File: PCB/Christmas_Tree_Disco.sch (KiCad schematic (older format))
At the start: 0 parts

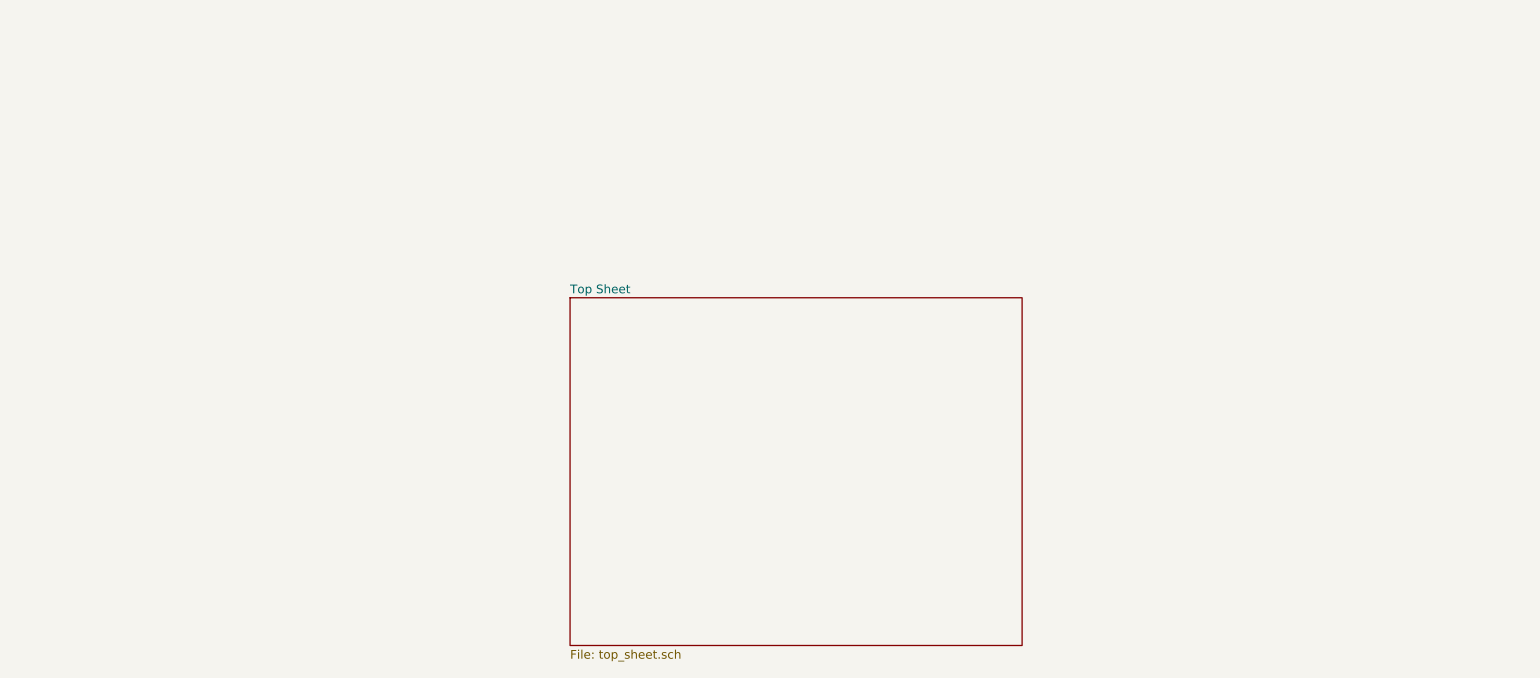
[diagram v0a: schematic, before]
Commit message: PCB Edge.Cuts Defined
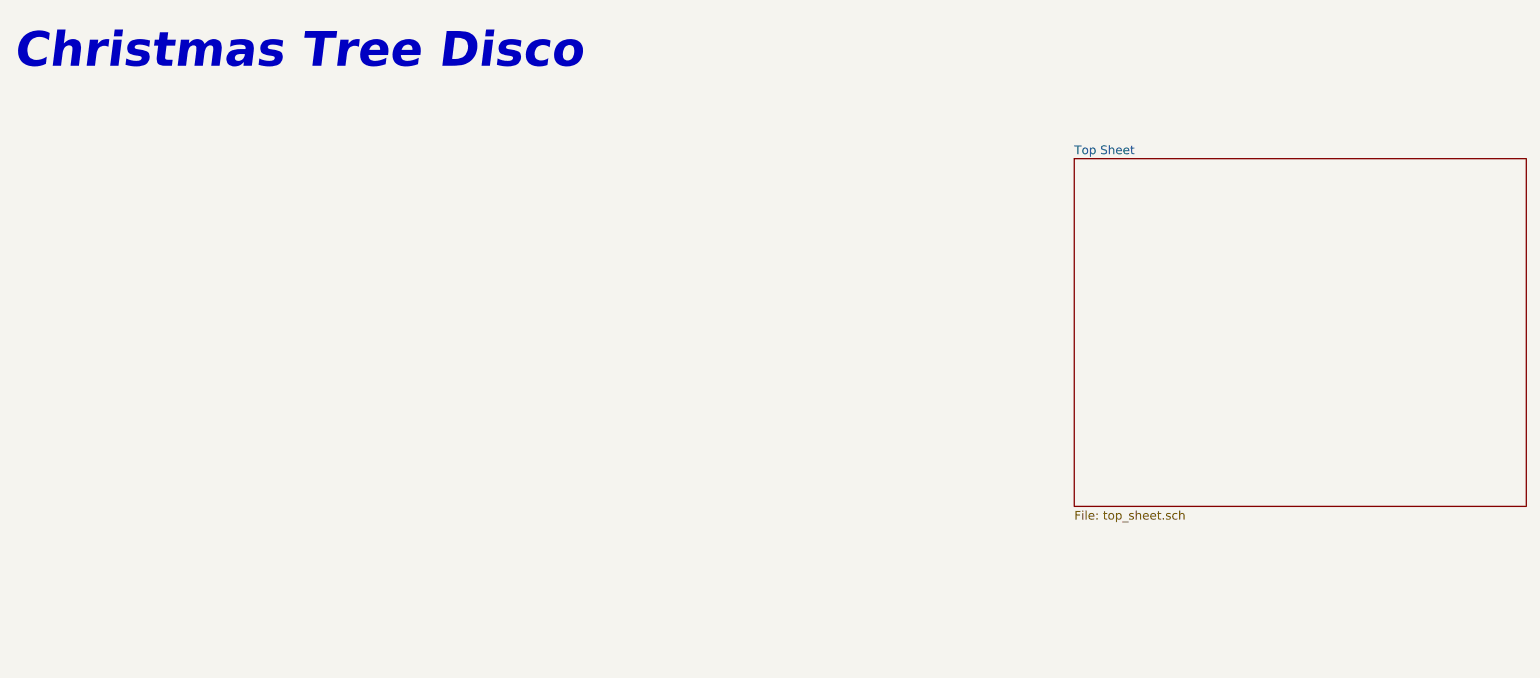
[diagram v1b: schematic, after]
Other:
- note added: "Christmas Tree Disco"
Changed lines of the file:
@@
 $Descr A 11000 8500
 encoding utf-8
-Sheet 1 5
+Sheet 1 20
 Title "Christmas Tree Disco"
 Date "2017-08-01"
 Rev "01"
-Comp "GitHub/Cryochasm"
+Comp "www.GitHub.com/Cryochasm"
 Comment1 ""
 Comment2 ""
@@
 $EndDescr
 $Sheet
-S 4000 2400 2600 2000
+S 6900 1600 2600 2000
 U 59809489
 F0 "Top Sheet" 50
 F1 "top_sheet.sch" 50
 $EndSheet
+Text Notes 800  1100 0    200  Italic 40
+Christmas Tree Disco
 $EndSCHEMATC

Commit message: Preliminary PCB layout
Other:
- note added: "Revisions:"
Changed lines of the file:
@@
 Text Notes 800  1100 0    200  Italic 40
 Christmas Tree Disco
+Text Notes 1000 1400 0    50   ~ 0
+Revisions:
 $EndSCHEMATC

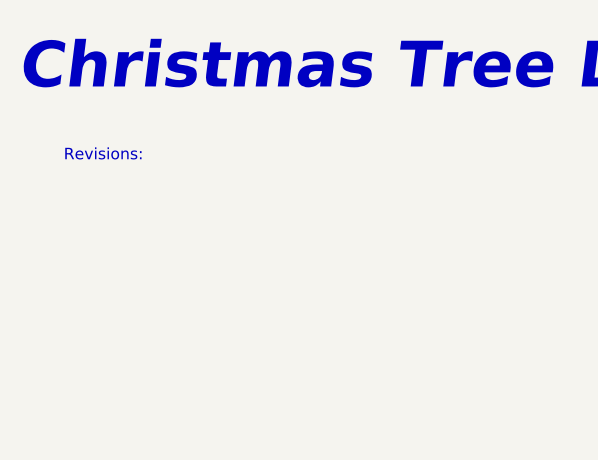
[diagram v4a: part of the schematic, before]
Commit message: V1.0 Ready for Review
Added compatability with the 430BOOST-C55AUDIO1 booster pack.
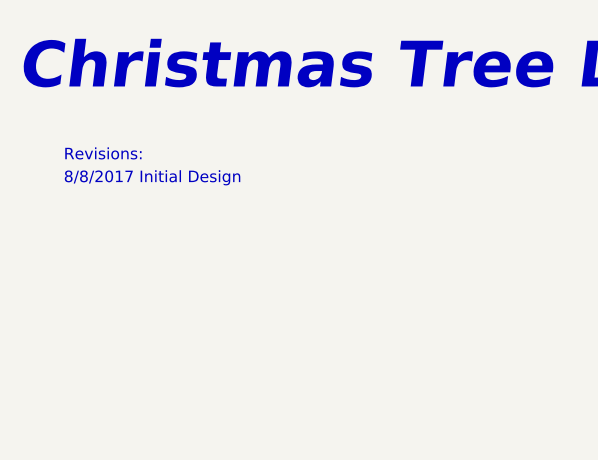
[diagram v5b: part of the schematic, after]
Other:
- note added: "8/8/2017 Initial Design"
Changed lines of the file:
@@
 Sheet 1 20
 Title "Christmas Tree Disco"
-Date "2017-08-01"
+Date "2017-08-08"
 Rev "01"
 Comp "www.GitHub.com/Cryochasm"
@@
 Text Notes 1000 1400 0    50   ~ 0
 Revisions:
+Text Notes 1000 1500 0    50   ~ 0
+8/8/2017 Initial Design
 $EndSCHEMATC

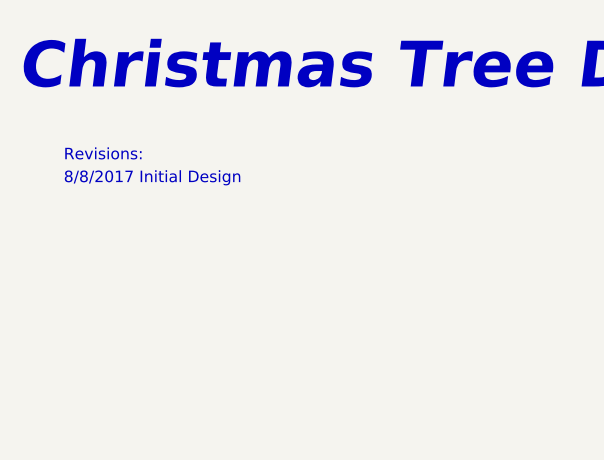
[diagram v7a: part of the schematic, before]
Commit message: Removed Level Shifter, Cleaned up gerbers
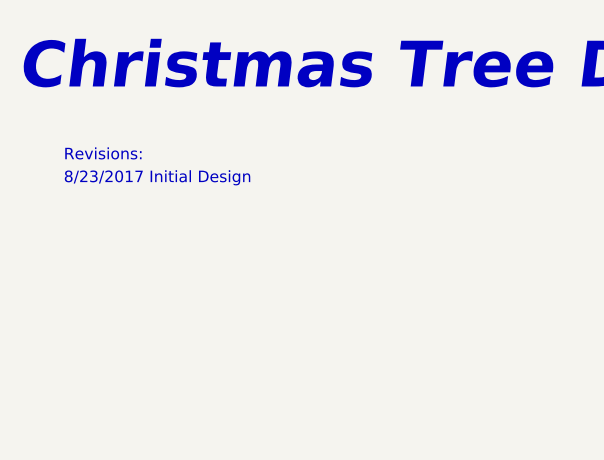
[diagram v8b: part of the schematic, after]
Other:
- note added: "8/23/2017 Initial Design"
- note removed: "8/8/2017 Initial Design"
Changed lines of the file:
@@
 Sheet 1 20
 Title "Christmas Tree Disco"
-Date "2017-08-15"
+Date "2017-08-23"
 Rev "V1.0"
 Comp "www.GitHub.com/Cryochasm"
@@
 Revisions:
 Text Notes 1000 1500 0    50   ~ 0
-8/8/2017 Initial Design
+8/23/2017 Initial Design
 $Bitmap
 Pos 9900 6100
